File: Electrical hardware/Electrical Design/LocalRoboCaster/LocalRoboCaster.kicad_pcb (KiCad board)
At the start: 2 copper layers, 100 x 83 mm, 72 parts, among them J1 Conn_01x06_Pin, J2 Conn_01x02_Pin, J3 voltage_in, J4 Conn_01x04_Pin, J5 Conn_01x04_Pin, J6 voltage_in, J7 voltage_in, J8 Conn_01x06_Pin, M1 Fan, M2 Stepper_Motor_bipolar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

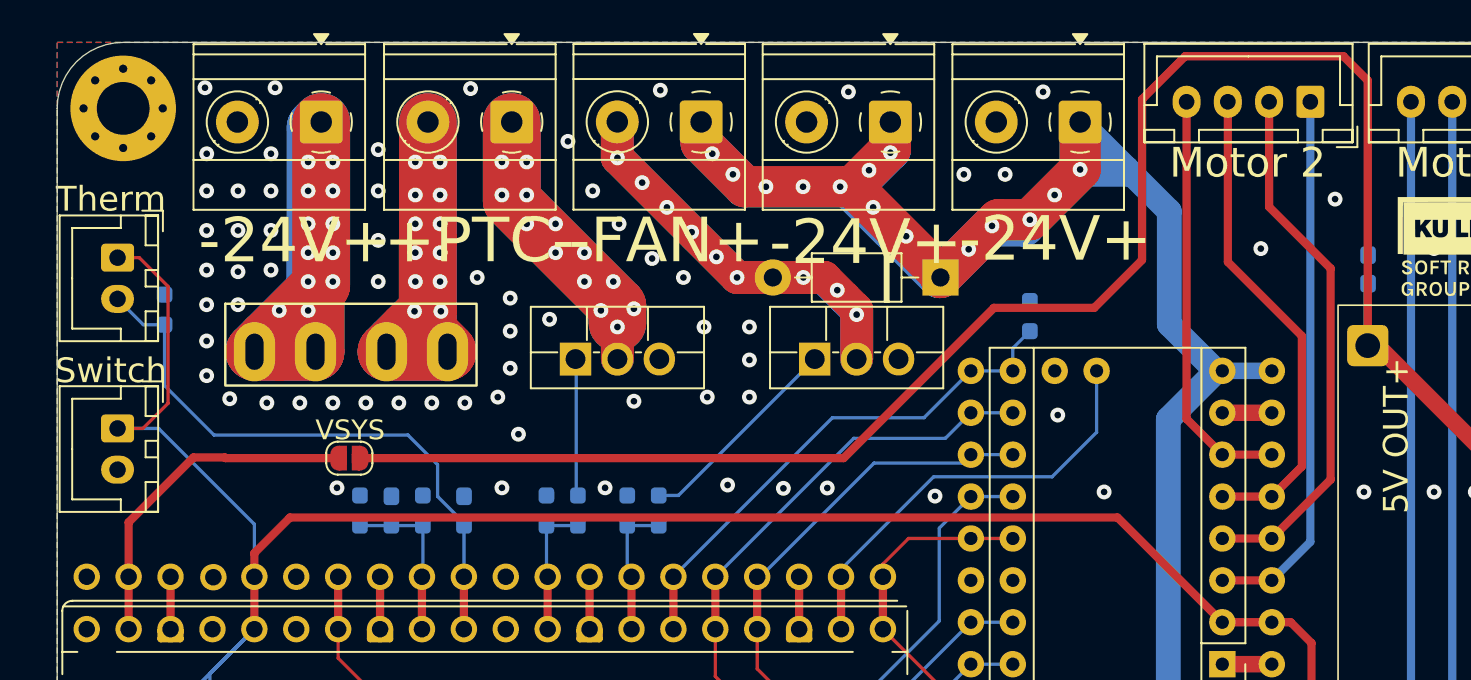
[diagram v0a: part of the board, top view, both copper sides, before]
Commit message: Added report and improved electrical design files
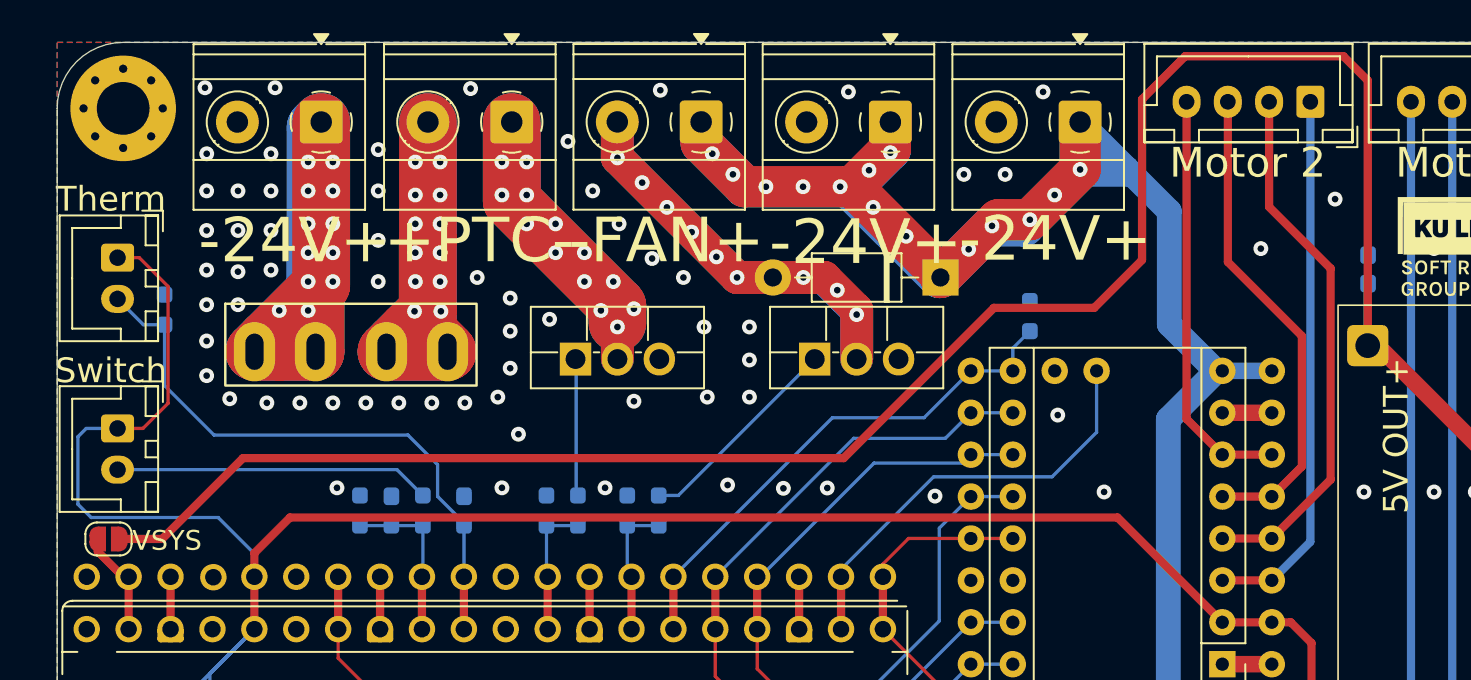
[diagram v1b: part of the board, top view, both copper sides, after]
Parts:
- moved JP5V7 15.4 mm to (44.6, 63.1)
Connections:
- R3 pad 2: /Data In And Out/switch_nc -> Net-(U3-no)
- U3 pad 2: unconnected-(U3-no-Pad2) -> Net-(U3-no)
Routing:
- net Net-(U3-no): track 0.00 -> 19.2 mm
- net +5V5: track 255.7 -> 272.3 mm
- net Net-(A1-VSYS): track 20.8 -> 6.44 mm
- net +3.3V: track 257.3 -> 263.4 mm
